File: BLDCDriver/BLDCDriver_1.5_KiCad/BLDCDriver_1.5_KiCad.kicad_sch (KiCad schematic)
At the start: 64 parts, among them IC1 STSPIN32G4, J2 Debug, J2 Motor Out, J4 POWER, J5 CAN, SW1 SW_Push, U3 MCP2562-E-SN, U5 AS5048A-HTSP-500, U6 AP7375-33SA-7

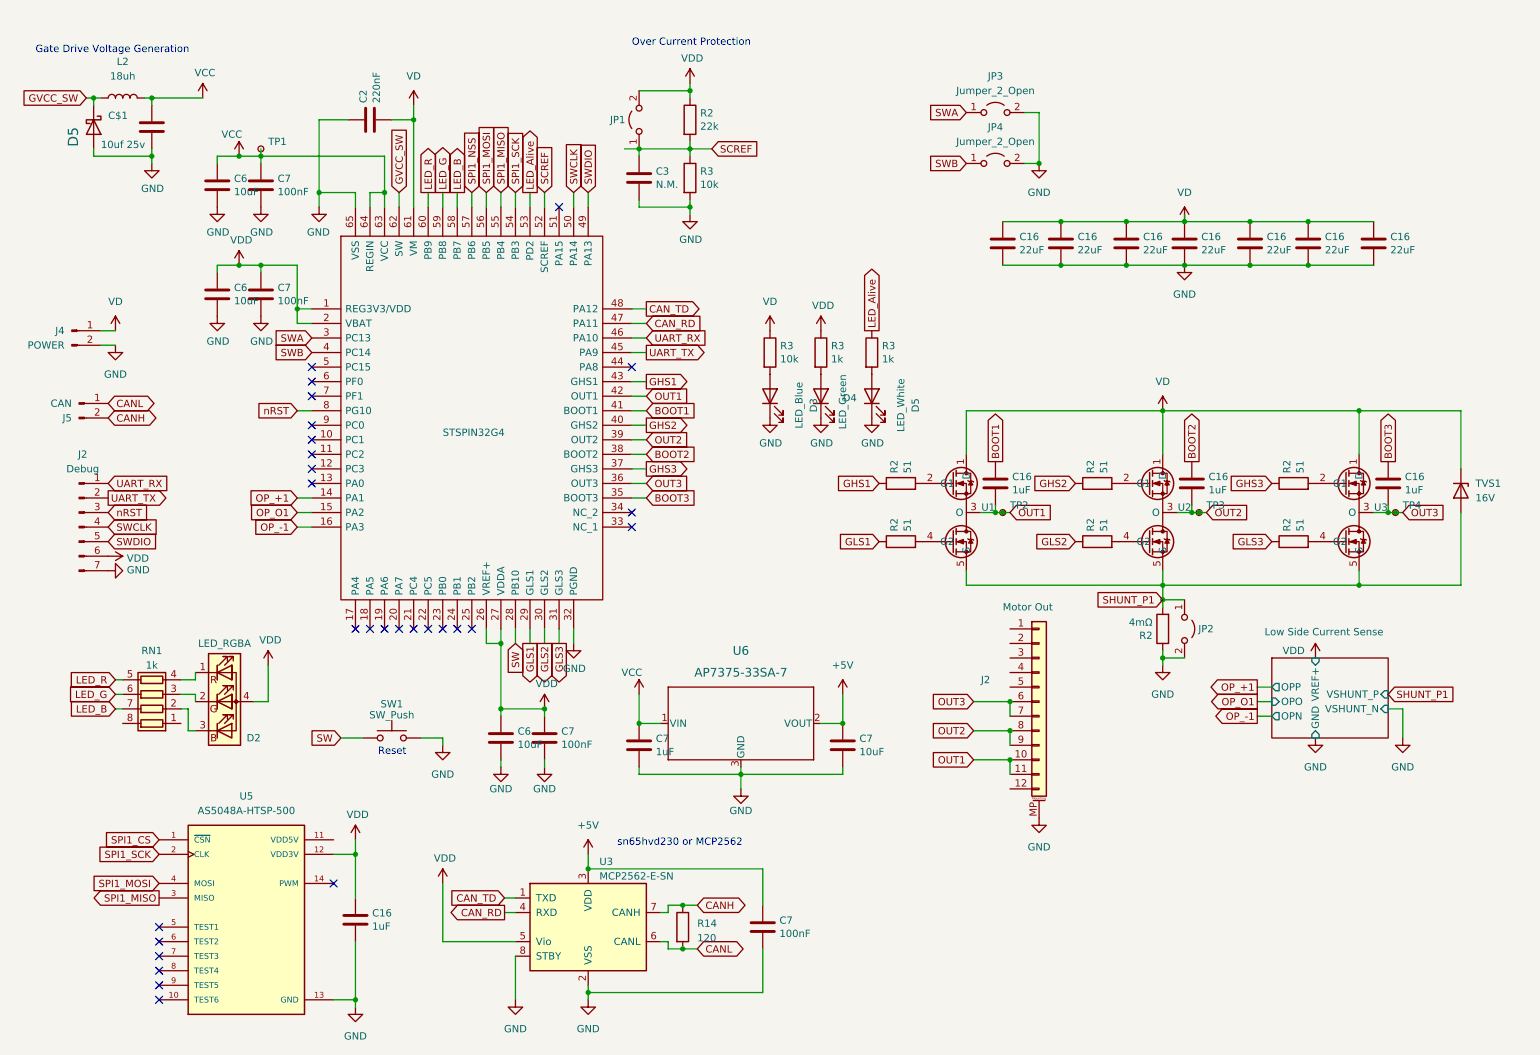
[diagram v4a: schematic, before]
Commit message: ✨UARTで受信できる保険をかけた
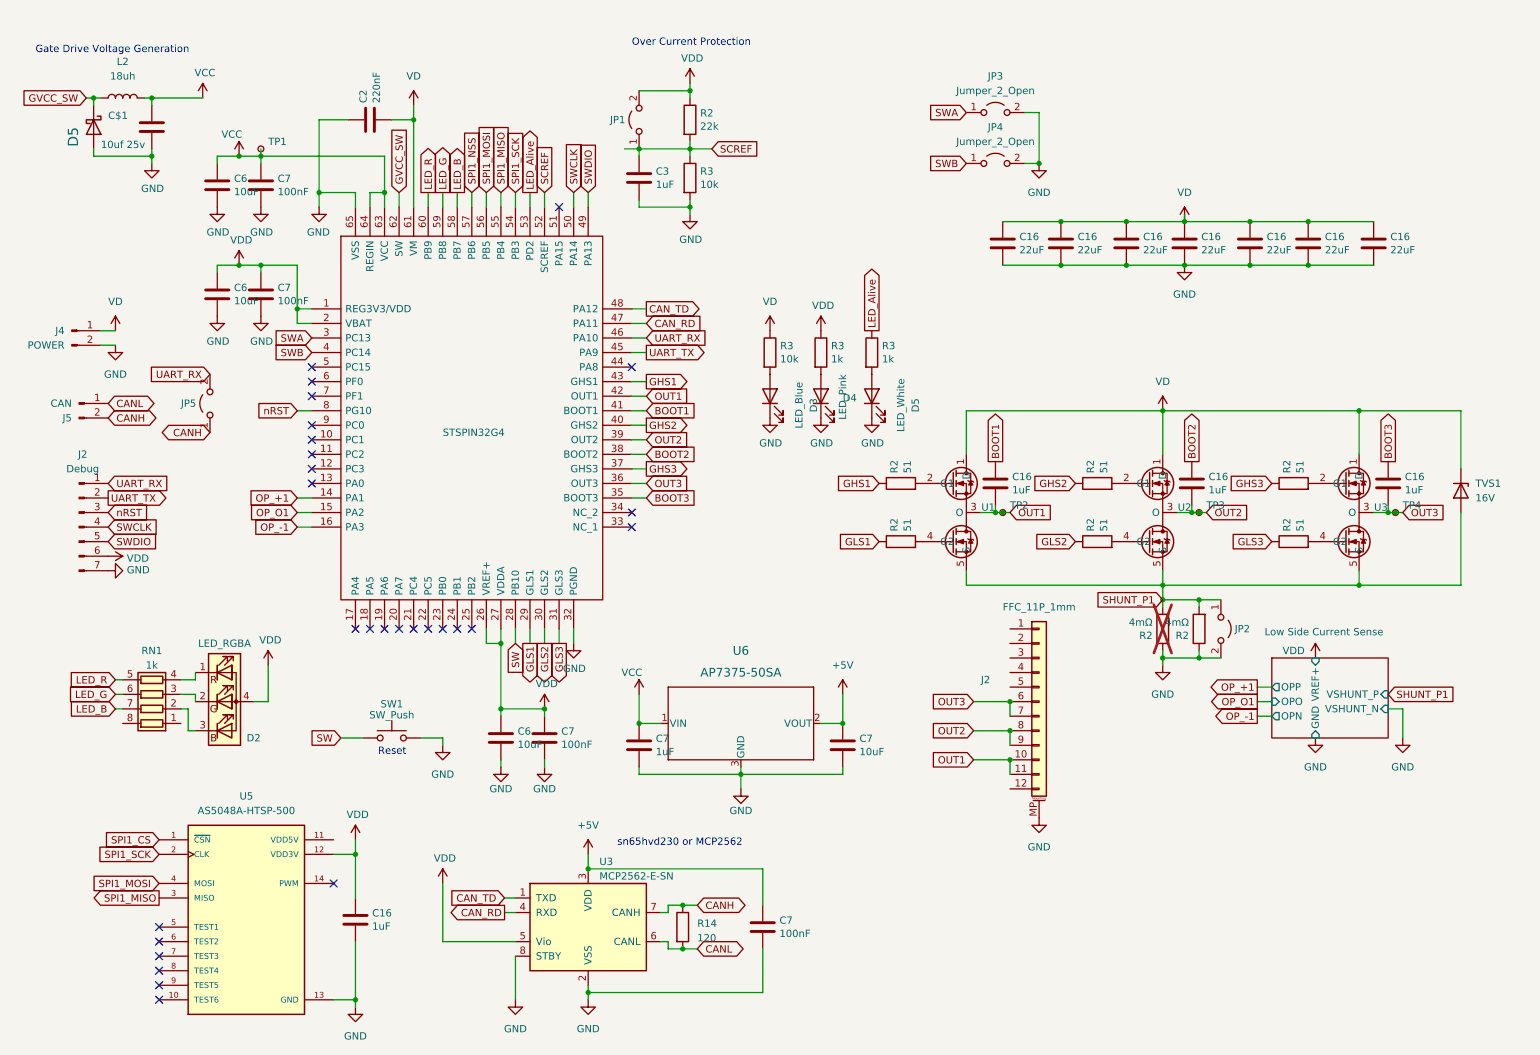
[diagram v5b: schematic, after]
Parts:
- added JP5: Jumper_2_Open, Jumper:SolderJumper-2_P1.3mm_Open_RoundedPad1.0x1.5mm, symbol Jumper:Jumper_2_Open
- added R2: 4mΩ, Resistor_SMD:R_2512_6332Metric, symbol Device:R
- C$1: LCSC (none) -> C15850; LCSC Part (none) -> C15850
- C16: LCSC (none) -> C338080
- C16: LCSC (none) -> C307413; LCSC Part C28323 -> C307413
- C2: LCSC (none) -> C107131; LCSC Part (none) -> C107131
- C3: value N.M. -> 1uF; LCSC (none) -> C307413; LCSC Part (none) -> C307413
- C6: LCSC (none) -> C15525; LCSC Part C15850 -> C15525
- C6: LCSC (none) -> C15525; LCSC Part C1524 -> C15525
- C7: LCSC (none) -> C15525; LCSC Part C7393877 -> C15525
- C7: LCSC (none) -> C131394; LCSC Part C7393877 -> C131394
- C7: LCSC (none) -> C307413; LCSC Part C7393877 -> C307413
- D2: LCSC (none) -> C2843813; LCSC Part (none) -> C2843813
- D3: LCSC (none) -> C965799; LCSC Part (none) -> C965799
- D4: value LED_Green -> LED_Pink; LCSC (none) -> C2977076; LCSC Part (none) -> C2977076
- D5: LCSC (none) -> C965808; LCSC Part (none) -> C965808
- D5: LCSC Part (none) -> C14996
- IC1: LCSC (none) -> C7434864; LCSC Part (none) -> C7434864
- J2: value Motor Out -> FFC_11P_1mm; LCSC (none) -> C2914070; LCSC Part (none) -> C2914070
- J5: LCSC (none) -> C3021286; LCSC Part (none) -> C3021286
- JP1, JP2, JP3, JP4, RN1: LCSC (none) -> C20197; LCSC Part (none) -> C20197
- L2: LCSC Part (none) -> C467143
- R14, TP1, TP2, TP3, TP4: LCSC (none) -> C22787; LCSC Part (none) -> C22787
- R2: LCSC (none) -> C25125; LCSC Part C31850 -> C25125
- R2: LCSC (none) -> C325408; LCSC Part C31850 -> C325408
- R2: LCSC (none) -> C5121077; LCSC Part C31850 -> C5121077; now not fitted
- R3: LCSC (none) -> C11702; LCSC Part C25804 -> C11702
- R3: LCSC (none) -> C25744; LCSC Part C25804 -> C25744
- SW1: LCSC Part (none) -> C3021286
- TVS1: LCSC (none) -> C25744; LCSC Part (none) -> C25744
- U1, U2, U3: LCSC (none) -> C25768; LCSC Part (none) -> C25768
- U3: LCSC (none) -> C53609; LCSC Part (none) -> C53609
- U6: value AP7375-33SA-7 -> AP7375-50SA; LCSC (none) -> C6500991; LCSC Part (none) -> C6500991
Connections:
- net CANH: now also JP5.1 (A)
- net GND: now also R2.1
- net SHUNT_P1: now also R2.2
- net UART_RX: now also JP5.2 (B)
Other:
- moved on the sheet: JP2

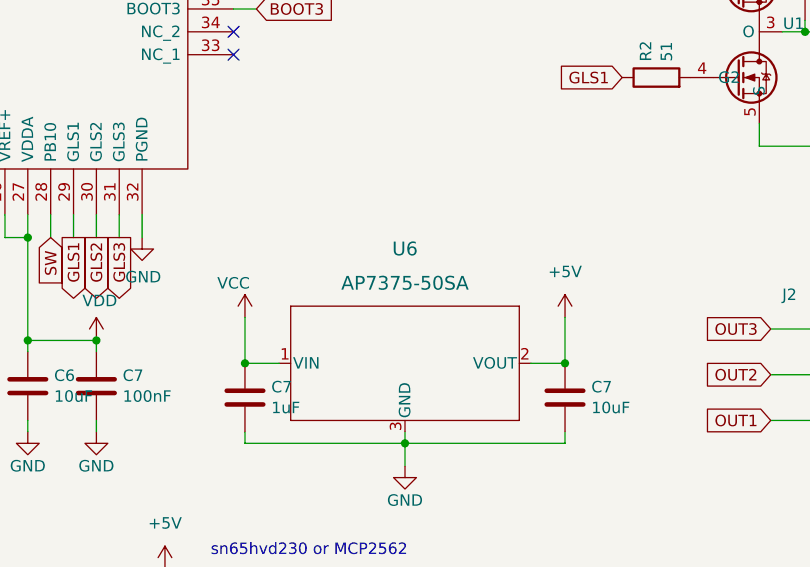
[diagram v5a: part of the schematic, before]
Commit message: ✨ プロダクションを途中まで進めた
MOSFETの発注が滞っているので、処理します
MOSFET、何故か10個からしか購入できないところで15個で購入しており、問題発生。30か20で購入しましょう
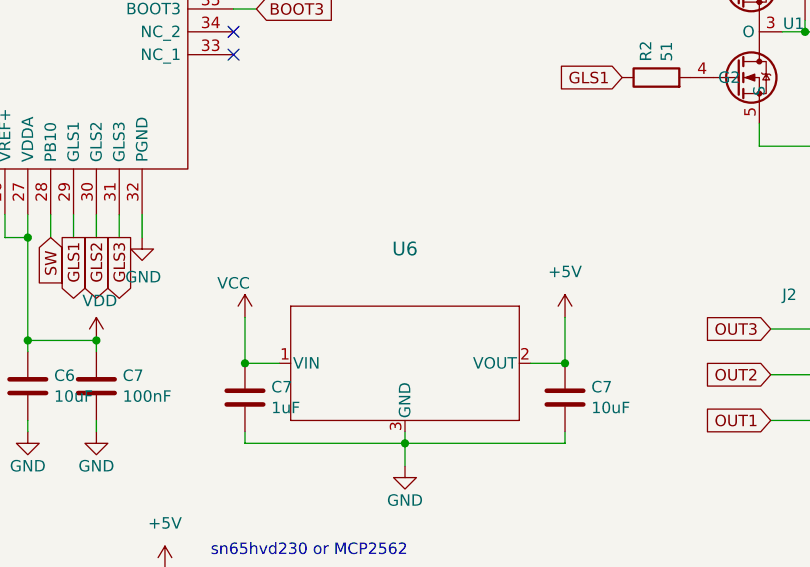
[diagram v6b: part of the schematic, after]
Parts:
- U1, U2, U3: LCSC C25768 -> (none); LCSC Part C25768 -> (none)
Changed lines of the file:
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@@
     )
     (property "Value" "AP7375-50SA" (at 143.51 129.54 0)
-      (effects (font (size 1.524 1.524)))
+      (effects (font (size 1.524 1.524)) hide)
     )
     (property "Footprint" "AP7375-33SA-7_DIO" (at 123.19 137.16 0)
@@
       (effects (font (size 1.27 1.27)) hide)
     )
-    (property "LCSC" "C25768" (at 251.46 101.6 0)
-      (effects (font (size 1.27 1.27)) hide)
-    )
-    (property "LCSC Part" "C25768" (at 251.46 101.6 0)
+    (property "LCSC" "" (at 251.46 101.6 0)
+      (effects (font (size 1.27 1.27)) hide)
+    )
+    (property "LCSC Part" "" (at 251.46 101.6 0)
       (effects (font (size 1.27 1.27)) hide)
     )
@@
       (effects (font (size 1.27 1.27)) hide)
     )
-    (property "LCSC" "C25768" (at 182.88 101.6 0)
-      (effects (font (size 1.27 1.27)) hide)
-    )
-    (property "LCSC Part" "C25768" (at 182.88 101.6 0)
+    (property "LCSC" "" (at 182.88 101.6 0)
+      (effects (font (size 1.27 1.27)) hide)
+    )
+    (property "LCSC Part" "" (at 182.88 101.6 0)
       (effects (font (size 1.27 1.27)) hide)
     )
@@
       (effects (font (size 1.27 1.27)) hide)
     )
-    (property "LCSC" "C25768" (at 217.17 101.6 0)
-      (effects (font (size 1.27 1.27)) hide)
-    )
-    (property "LCSC Part" "C25768" (at 217.17 101.6 0)
-      (effects (font (size 1.27 1.27)) hide)
-    )
+    (property "LCSC" "" (at 217.17 101.6 0)
+      (effects (font (size 1.27 1.27)) hide)
+    )
+    (property "LCSC Part" "" (at 217.17 101.6 0)
+      (effects (font (size 1.27 1.27)) hide)
+    )

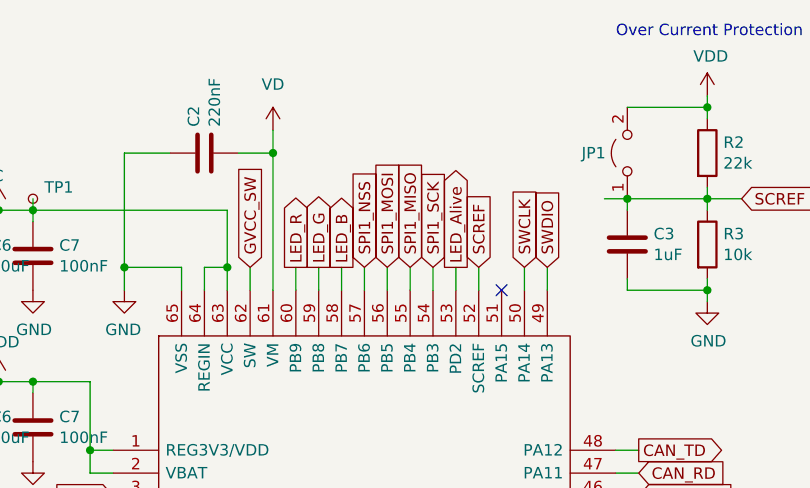
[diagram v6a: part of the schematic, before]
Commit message: ⚠️PB8_BOOT0をGNDに落とした
データシート読まないと...
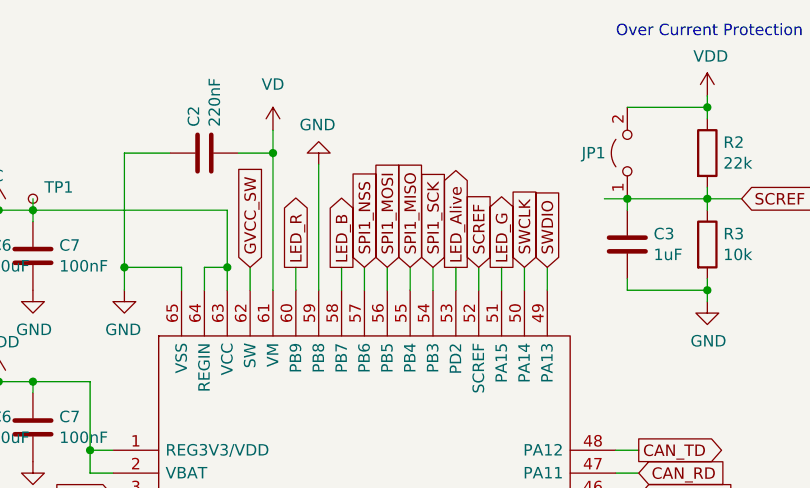
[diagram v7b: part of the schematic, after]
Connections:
- net GND: now also IC1.59 (PB8)
- net LED_G: now also IC1.51 (PA15); no longer IC1.59 (PB8)
- no-connect marks 28 -> 27
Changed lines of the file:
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@@
   )
   (no_connect (at 96.52 121.92))
-  (no_connect (at 111.76 48.26))
   (no_connect (at 86.36 121.92))
   (no_connect (at 124.46 104.14))
@@
     (stroke (width 0) (type default))
   )
-  (wire (pts (xy 91.44 48.26) (xy 91.44 45.72))
-    (stroke (width 0) (type default))
-  )
   (wire (pts (xy 199.39 58.42) (xy 210.82 58.42))
     (stroke (width 0) (type default))
@@
     (stroke (width 0) (type default))
   )
+  (wire (pts (xy 111.76 48.26) (xy 111.76 45.72))
+    (stroke (width 0) (type default))
+  )
   (wire (pts (xy 104.14 45.72) (xy 104.14 48.26))
     (stroke (width 0) (type default))
@@
   )
   (wire (pts (xy 242.57 50.8) (xy 254 50.8))
+    (stroke (width 0) (type default))
+  )
+  (wire (pts (xy 91.44 34.29) (xy 91.44 48.26))
     (stroke (width 0) (type default))
   )
@@
     )
   )
+  (global_label "LED_G" (shape output) (at 111.76 45.72 90) (fields_autoplaced)
+    (effects (font (size 1.27 1.27)) (justify left))
+    (property "Intersheetrefs" "${INTERSHEET_REFS}" (at 111.76 37.4669 90)
+      (effects (font (size 1.27 1.27)) (justify left) hide)
+    )
+  )
   (global_label "BOOT2" (shape input) (at 127 91.44 0) (fields_autoplaced)
     (effects (font (size 1.27 1.27)) (justify left))
@@
     (effects (font (size 1.27 1.27)) (justify left))
     (property "Intersheetrefs" "${INTERSHEET_REFS}" (at 41.2863 85.09 0)
-      (effects (font (size 1.27 1.27)) (justify left) hide)
-    )
-  )
-  (global_label "LED_G" (shape output) (at 91.44 45.72 90) (fields_autoplaced)
-    (effects (font (size 1.27 1.27)) (justify left))
-    (property "Intersheetrefs" "${INTERSHEET_REFS}" (at 91.44 37.4669 90)
       (effects (font (size 1.27 1.27)) (justify left) hide)
     )
@@
         )
       )
+    )
+  )
+  (symbol (lib_id "power:GND") (at 91.44 34.29 180) (unit 1)
+    (in_bom yes) (on_board yes) (dnp no)
+    (property "Reference" "#PWR0118" (at 91.44 27.94 0)
+      (effects (font (size 1.27 1.27)) hide)
+    )
+    (property "Value" "GND" (at 91.313 29.8958 0)
+      (effects (font (size 1.27 1.27)))
+    )
+    (property "Footprint" "" (at 91.44 34.29 0)
+      (effects (font (size 1.27 1.27)) hide)
+    )
+    (property "Datasheet" "" (at 91.44 34.29 0)
+      (effects (font (size 1.27 1.27)) hide)
+    )
+    (pin "1")
+    (instances
+      (project "STSPIN32G4"
+        (path "/385aece2-0a9a-427b-b04e-5177991aa74a"
+          (reference "#PWR0118") (unit 1)
+        )
+      )
+      (project "BLDCDriver_1.5_KiCad"
+        (path "/7b455adc-1ddb-4b8a-b7cd-7eada40acc4a"
+          (reference "#PWR046") (unit 1)
+        )
+      )

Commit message: ✨Productionファイル生成した
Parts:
- SW1: LCSC C3021286 -> C2888433; LCSC Part C3021286 -> C2888433
- U1, U2, U3: LCSC (none) -> C7503829; LCSC Part (none) -> C7503829
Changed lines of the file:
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@@
       (effects (font (size 1.27 1.27)) hide)
     )
-    (property "LCSC" "" (at 251.46 101.6 0)
-      (effects (font (size 1.27 1.27)) hide)
-    )
-    (property "LCSC Part" "" (at 251.46 101.6 0)
+    (property "LCSC" "C7503829" (at 251.46 101.6 0)
+      (effects (font (size 1.27 1.27)) hide)
+    )
+    (property "LCSC Part" "C7503829" (at 251.46 101.6 0)
       (effects (font (size 1.27 1.27)) hide)
     )
@@
       (effects (font (size 1.27 1.27)) hide)
     )
-    (property "Datasheet" "https://datasheet.lcsc.com/lcsc/2206281830_SOFNG-TS-1808S-16_C3021286.pdf" (at 82.55 135.89 0)
-      (effects (font (size 1.27 1.27)) hide)
-    )
-    (property "LCSC" "C3021286" (at 82.55 140.97 0)
-      (effects (font (size 1.27 1.27)) hide)
-    )
-    (property "LCSC Part" "C3021286" (at 82.55 140.97 0)
+    (property "Datasheet" "https://datasheet.lcsc.com/lcsc/2108261830_BZCN-TSA017A2526A_C2888433.pdf" (at 82.55 135.89 0)
+      (effects (font (size 1.27 1.27)) hide)
+    )
+    (property "LCSC" "C2888433" (at 82.55 140.97 0)
+      (effects (font (size 1.27 1.27)) hide)
+    )
+    (property "LCSC Part" "C2888433" (at 82.55 140.97 0)
       (effects (font (size 1.27 1.27)) hide)
     )
@@
       (effects (font (size 1.27 1.27)) hide)
     )
-    (property "LCSC" "" (at 182.88 101.6 0)
-      (effects (font (size 1.27 1.27)) hide)
-    )
-    (property "LCSC Part" "" (at 182.88 101.6 0)
+    (property "LCSC" "C7503829" (at 182.88 101.6 0)
+      (effects (font (size 1.27 1.27)) hide)
+    )
+    (property "LCSC Part" "C7503829" (at 182.88 101.6 0)
       (effects (font (size 1.27 1.27)) hide)
     )
@@
       (effects (font (size 1.27 1.27)) hide)
     )
-    (property "LCSC" "" (at 217.17 101.6 0)
-      (effects (font (size 1.27 1.27)) hide)
-    )
-    (property "LCSC Part" "" (at 217.17 101.6 0)
-      (effects (font (size 1.27 1.27)) hide)
-    )
+    (property "LCSC" "C7503829" (at 217.17 101.6 0)
+      (effects (font (size 1.27 1.27)) hide)
+    )
+    (property "LCSC Part" "C7503829" (at 217.17 101.6 0)
+      (effects (font (size 1.27 1.27)) hide)
+    )
